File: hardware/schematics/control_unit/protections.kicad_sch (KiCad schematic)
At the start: 6 parts, among them U16 LM35-D, U17 LM358

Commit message: feat
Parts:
- removed U17: LM358, symbol Amplifier_Operational:LM358
- added U18: LM324, Package_DIP:DIP-14_W7.62mm_Socket, symbol Amplifier_Operational:LM324
- C6: footprint (none) -> Capacitor_THT:C_Rect_L7.2mm_W2.5mm_P5.00mm_FKS2_FKP2_MKS2_MKP2
- R52: renamed from R49; footprint (none) -> Resistor_THT:R_Axial_DIN0207_L6.3mm_D2.5mm_P7.62mm_Horizontal
- R53: renamed from R50; footprint (none) -> Resistor_THT:R_Axial_DIN0207_L6.3mm_D2.5mm_P7.62mm_Horizontal
- R54: renamed from R51; footprint (none) -> Resistor_THT:R_Axial_DIN0207_L6.3mm_D2.5mm_P7.62mm_Horizontal
- renumbered U16 to U17
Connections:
- net 5V: now also U18.4 (V+)
- net GND: now also U18.11 (V-)
- net TEMP: now also U18.1
- net at C6.1, R52.2: now also U18.3 (+)
- net at R53.2, R54.1: now also U18.2 (-)
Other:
- moved on the sheet: C6, R52, R53, R54, U17

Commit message: !feat
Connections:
- net GND: now also R53.2; no longer R53.1
- net at R54.1, U18.2 (-): now also R53.1; no longer R53.2
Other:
- moved on the sheet: R53
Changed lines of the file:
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@@
 	(symbol
 		(lib_id "Device:R")
-		(at 151.13 80.01 90)
+		(at 151.13 80.01 270)
+		(mirror x)
 		(unit 1)
 		(exclude_from_sim no)

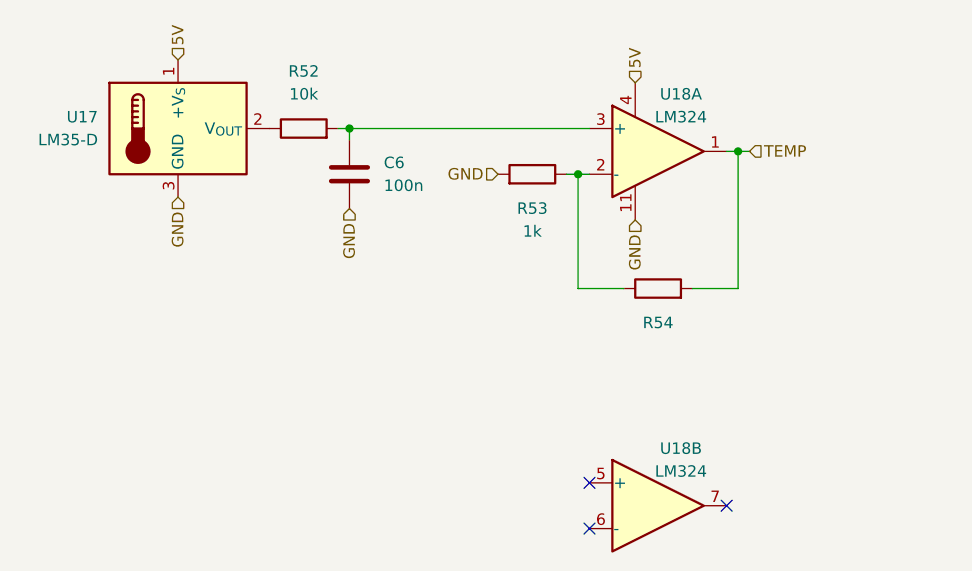
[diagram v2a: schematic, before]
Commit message: feat: added PowerMonitor resistor's values.
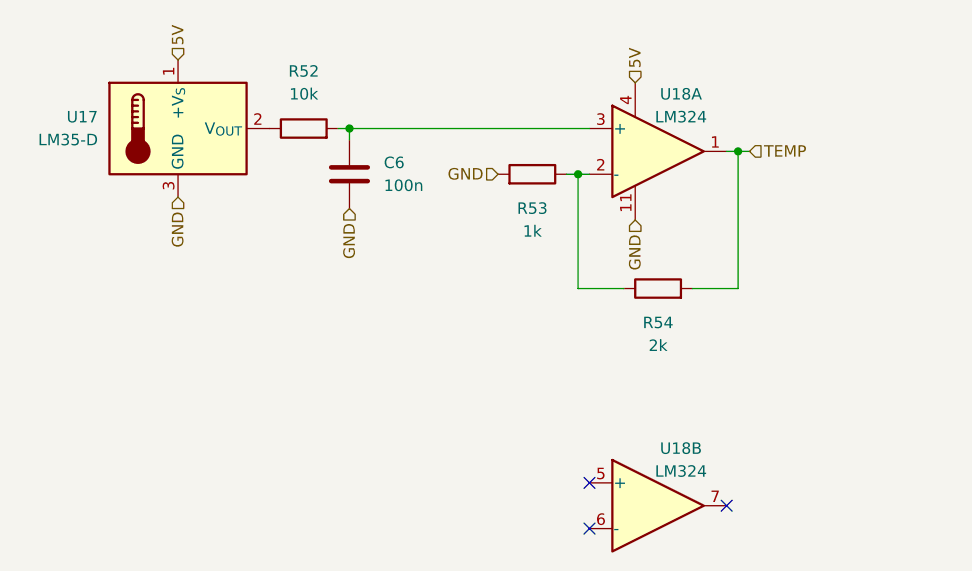
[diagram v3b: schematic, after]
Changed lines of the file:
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@@
 					(size 1.27 1.27)
 				)
-				(hide yes)
 			)
 		)
